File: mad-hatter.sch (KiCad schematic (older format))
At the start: 153 parts, among them U1 ATMEGA32U4, X1 XTAL_GND

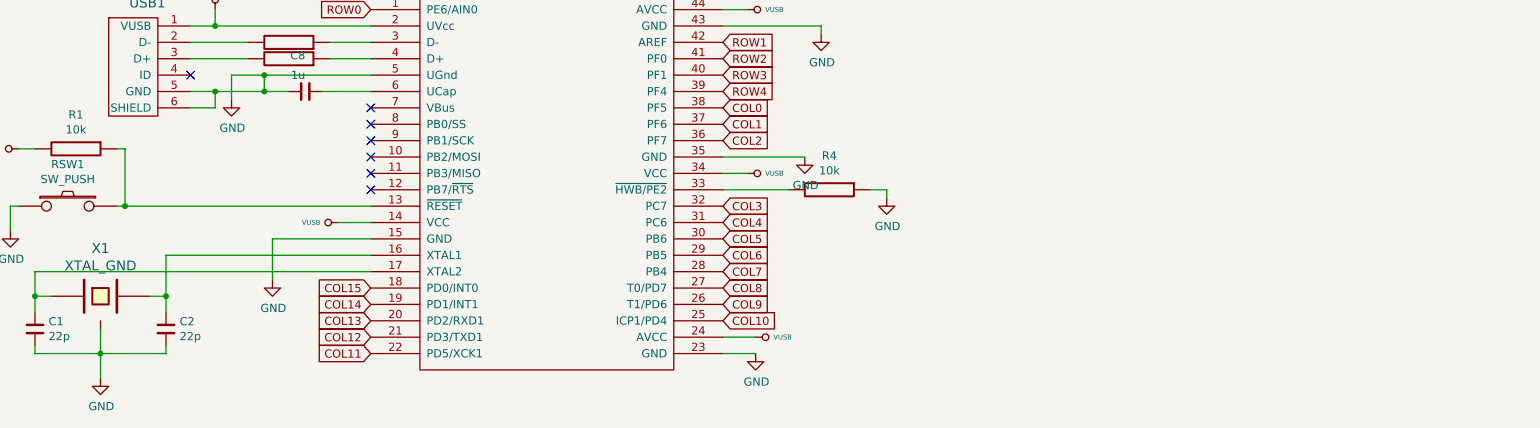
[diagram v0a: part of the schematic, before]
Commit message: Starts adding ISP pads
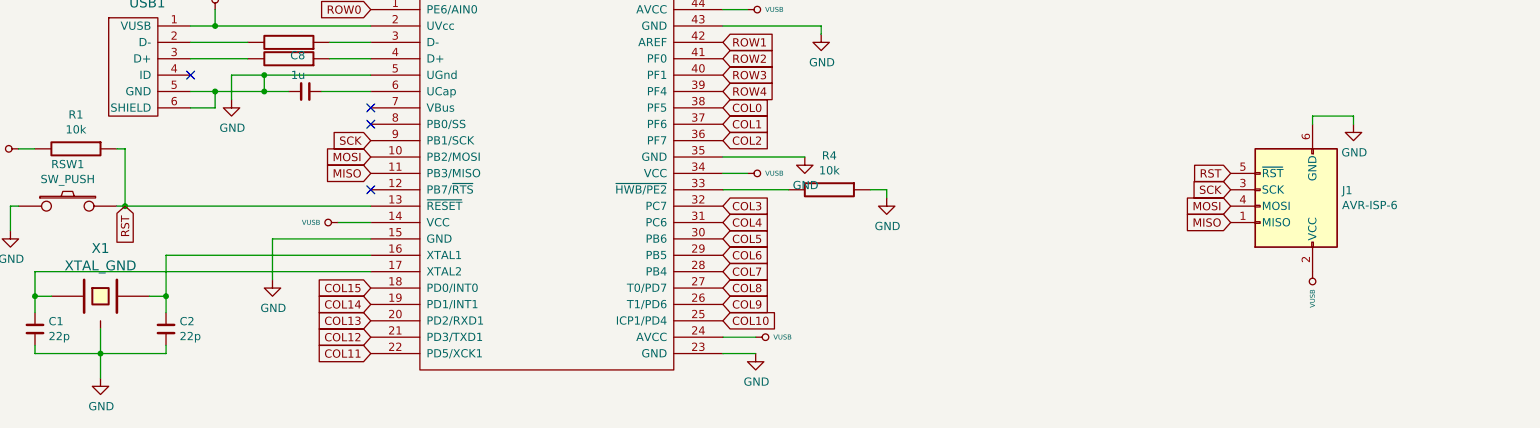
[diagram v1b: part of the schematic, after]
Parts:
- added J1: AVR-ISP-6, keyboard_parts:AVR_ICSP_3x2, symbol Connector:AVR-ISP-6
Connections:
- net GND: now also J1.6 (GND)
- net VUSB: now also J1.2 (VCC)
- net MOSI: now reaches U1.10 (PB2/MOSI)
- net MOSI: now also J1.4 (MOSI)
- net MISO: now reaches U1.11 (PB3/MISO)
- net MISO: now also J1.1 (MISO)
- net RST: now reaches R1.1, RSW1.2, U1.13 (~RESET)
- net RST: now also J1.5 (~RST)
- net SCK: now reaches U1.9 (PB1/SCK)
- net SCK: now also J1.3 (SCK)
- no-connect marks 7 -> 4
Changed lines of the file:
@@
 EESchema Schematic File Version 4
-LIBS:alice-cache
+LIBS:mad-hatter-cache
 EELAYER 26 0
 EELAYER END
@@
 NoConn ~ 4750 9300
 NoConn ~ 4750 9400
-NoConn ~ 4750 9500
-NoConn ~ 4750 9600
-NoConn ~ 4750 9700
 NoConn ~ 4750 9800
 NoConn ~ 3650 9100
@@
 	5550 4200 5550 5200
 Connection ~ 5550 4200
+$Comp
+L Connector:AVR-ISP-6 J1
+U 1 1 5C8BF2DB
+P 10400 9800
+F 0 "J1" H 10120 9804 50  0000 R CNN
+F 1 "AVR-ISP-6" H 10120 9895 50  0000 R CNN
+F 2 "keyboard_parts:AVR_ICSP_3x2" V 10150 9850 50  0001 C CNN
+F 3 " ~" H 9125 9250 50  0001 C CNN
+	1    10400 9800
+	-1   0    0    1
+$EndComp
+Text GLabel 4750 9500 0    50   Input ~ 0
+SCK
+Text GLabel 10000 9800 0    50   Input ~ 0
+SCK
+Text GLabel 10000 9900 0    50   Input ~ 0
+MOSI
+Text GLabel 10000 10000 0    50   Input ~ 0
+MISO
+Text GLabel 10000 9700 0    50   Input ~ 0
+RST
+$Comp
+L keyboard_parts:VUSB #PWR0117
+U 1 1 5C94BE31
+P 10500 10300
+F 0 "#PWR0117" H 10500 10270 20  0001 C CNN
+F 1 "VUSB" V 10500 10408 30  0000 L CNN
+F 2 "" H 10500 10300 60  0000 C CNN
+F 3 "" H 10500 10300 60  0000 C CNN
+	1    10500 10300
+	-1   0    0    1
+$EndComp
+Text GLabel 3250 9900 3    50   Input ~ 0
+RST
+Text GLabel 4750 9600 0    50   Input ~ 0
+MOSI
+Text GLabel 4750 9700 0    50   Input ~ 0
+MISO
+$Comp
+L power:GND #PWR?
+U 1 1 5CB0A415
+P 10750 9400
+F 0 "#PWR?" H 10750 9150 50  0001 C CNN
+F 1 "GND" H 10755 9227 50  0000 C CNN
+F 2 "" H 10750 9400 50  0001 C CNN
+F 3 "" H 10750 9400 50  0001 C CNN
+	1    10750 9400
+	1    0    0    -1
+$EndComp
+Wire Wire Line
+	10500 9400 10500 9350
+Wire Wire Line
+	10500 9350 10750 9350
+Wire Wire Line
+	10750 9350 10750 9400
 $EndSCHEMATC

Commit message: Fixes crystal connection; improves matrix; adds fuse
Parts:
- removed USB1: USB_mini_micro_B, keyboard_parts:USB_miniB_hirose_5S8, symbol keyboard_parts:USB_mini_micro_B
- added F1: 500mA, Fuse:Fuse_1206_3216Metric_Pad1.42x1.75mm_HandSolder, symbol Device:Polyfuse_Small
- added J1: XM7D-0512, OMRON_XM7D-0512, symbol XM7D-0512:XM7D-0512
- U1: footprint Package_DFN_QFN:QFN-44-1EP_7x7mm_P0.5mm_EP5.2x5.2mm -> keyboard_parts:QFP44_reflow
- X1: value XTAL_GND -> 16MHz; symbol keyboard_parts:XTAL_GND -> Device:Crystal_GND24
- renumbered J1 to J2
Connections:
- net VUSB is gone; now on net +5V: C3.1, C4.1, C5.1, C6.1, C7.1, J2.2 (VCC), R1.2, U1.14 (VCC), U1.2 (UVcc), U1.24 (AVCC), U1.34 (VCC), U1.44 (AVCC)
- net COL0: now also K_`1.1, U1.40 (PF1); no longer U1.38 (PF5)
- net COL1: now also K_1.1, U1.39 (PF4); no longer K_`1.1, U1.37 (PF6)
- net COL10: now also K_0.1, K_L1.1, K_O1.1; no longer K_9.1, K_I1.1, K_K1.1
- net COL11: now also K_MINUS1.1, K_P1.1, K_SEMIC1.1; no longer K_0.1, K_L1.1, K_O1.1
- net COL12: now also K_EQUAL1.1, K_QUOTE1.1, K_[1.1; no longer K_MINUS1.1, K_P1.1, K_SEMIC1.1
- net COL13: now also K_BACKSPACE1.1, K_BACKSPACE2.2, K_ENTER1.1, K_SHIFT2.1, K_SHIFT2_2.2, K_]1.1; no longer K_EQUAL1.1, K_QUOTE1.1, K_[1.1
- net COL14: now also K_13.1, K_BSLSH1.1, K_BSLSH2.1, K_CTRL2.1; no longer K_BACKSPACE1.1, K_BACKSPACE2.2, K_ENTER1.1, K_SHIFT2.1, K_SHIFT2_2.2, K_]1.1
- net COL2: now also K_2.1, U1.38 (PF5); no longer K_1.1, U1.36 (PF7)
- net COL3: now also K_3.1; no longer K_2.1
- net COL4: now also K_4.1; no longer K_3.1
- net COL5: now also K_5.1; no longer K_4.1
- net COL6: now also K_6.1; no longer K_5.1
- net COL7: now also K_7.1, K_H1.1, K_Y1.1; no longer K_6.1
- net COL8: now also K_8.1, K_J1.1, K_U1.1; no longer K_7.1, K_H1.1, K_Y1.1
- net COL9: now also K_9.1, K_I1.1, K_K1.1; no longer K_8.1, K_J1.1, K_U1.1
- net GND: now also X1.2, X1.4, J1.5, J1.SH1 (SHIELD), J1.SH2 (SHIELD), J1.SH3 (SHIELD), J1.SH4 (SHIELD); no longer X1.3
- net ROW0: no longer D_PRSCR1.1 (K)
- net ROW1: now also D_PRSCR1.1 (K), U1.8 (PB0/SS); no longer D_PGUP1.1 (K), U1.42 (AREF)
- net ROW2: now also D_PGUP1.1 (K); no longer D_PGDN1.1 (K)
- net ROW3: now also D_PGDN1.1 (K), U1.37 (PF6); no longer U1.40 (PF1)
- net ROW4: now also U1.36 (PF7); no longer U1.39 (PF4)
- net at C1.1, X1.1: now also U1.16 (XTAL1); no longer U1.17 (XTAL2)
- net +5V: now reaches U1.7 (VBus)
- net +5V: now also F1.1
- net at R2.2: now also J1.2
- net at R3.2: now also J1.3
- removed net COL15: K_13.1, K_BSLSH1.1, K_BSLSH2.1, K_CTRL2.1, U1.18 (PD0/INT0)
- new net: C2.1, U1.17 (XTAL2), X1.3
- new net VCC: F1.2, J1.1
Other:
- moved on the sheet: C1, C2, D_1, D_12, D_2, D_3, D_4, D_5, D_6, D_ALT2, D_B2, D_COMMA1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
